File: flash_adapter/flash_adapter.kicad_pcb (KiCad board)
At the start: 2 copper layers, 47 x 53.3 mm, 4 parts, among them J1 Conn_02x12_Odd_Even, J2 Conn_02x12_Odd_Even, J4 Conn_01x04_Pin, U1 Kickstart_Socket_A4000

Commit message: finish routing
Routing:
- net /L18: track 0.00 -> 45.9 mm, vias 0 -> 1
- net /L8: track 0.00 -> 45.5 mm, vias 0 -> 1
- net /R15: track 0.00 -> 44.8 mm, vias 0 -> 2
- net /R16: track 0.00 -> 43.1 mm, vias 0 -> 2
- net /L7: track 0.00 -> 43.0 mm, vias 0 -> 1
- net /R24: track 0.00 -> 42.7 mm, vias 0 -> 2
- net /L20: track 0.00 -> 40.6 mm, vias 0 -> 1
- net /R21: track 0.00 -> 40.2 mm, vias 0 -> 2
- net /L6: track 0.00 -> 39.6 mm, vias 0 -> 2
- net /L17: track 0.00 -> 38.1 mm, vias 0 -> 1
- net /L5: track 0.00 -> 37.9 mm, vias 0 -> 2
- net /L22: track 0.00 -> 37.9 mm, vias 0 -> 2
- net /R17: track 0.00 -> 36.7 mm, vias 0 -> 2
- net /R23: track 15.1 -> 51.2 mm, vias 0 -> 2
- net /L12: track 0.00 -> 35.7 mm, vias 0 -> 1
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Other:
- board text added: "1"

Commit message: increase silkscreen line width; manufacturability
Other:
- board text added: "Flashrom programming adapter"
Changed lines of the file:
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@@
     )
     (pad_to_mask_clearance 0)
+    (aux_axis_origin 79.375 66.04)
     (pcbplotparams
-      (layerselection 0x00010fc_ffffffff)
+      (layerselection 0x00010ec_ffffffff)
       (plot_on_all_layers_selection 0x0000000_00000000)
       (disableapertmacros false)
-      (usegerberextensions false)
-      (usegerberattributes true)
-      (usegerberadvancedattributes true)
-      (creategerberjobfile true)
+      (usegerberextensions true)
+      (usegerberattributes false)
+      (usegerberadvancedattributes false)
+      (creategerberjobfile false)
       (dashed_line_dash_ratio 12.000000)
       (dashed_line_gap_ratio 3.000000)
@@
       (psa4output false)
       (plotreference true)
-      (plotvalue true)
+      (plotvalue false)
       (plotinvisibletext false)
       (sketchpadsonfab false)
-      (subtractmaskfromsilk false)
+      (subtractmaskfromsilk true)
       (outputformat 1)
       (mirror false)
-      (drillshape 1)
+      (drillshape 0)
       (scaleselection 1)
-      (outputdirectory "")
+      (outputdirectory "output/")
     )
   )
@@
     (property "ki_keywords" "ROM SOKCET")
     (attr through_hole)
-    (fp_text reference "U1" (at 7.62 2.54) (layer "F.SilkS")
+    (fp_text reference "U1" (at 7.62 2.54 unlocked) (layer "F.SilkS")
         (effects (font (size 1 1) (thickness 0.15)))
     )
@@
     (property "ki_keywords" "connector")
     (attr through_hole)
-    (fp_text reference "J2" (at -1.27 31.115) (layer "F.SilkS")
+    (fp_text reference "J2" (at -1.27 31.115 unlocked) (layer "F.SilkS")
         (effects (font (size 1 1) (thickness 0.15)))
     )
@@
     (property "ki_keywords" "connector")
     (attr through_hole)
-    (fp_text reference "J4" (at 2.79 3.81 -180) (layer "F.SilkS")
+    (fp_text reference "J4" (at 2.79 3.81 unlocked) (layer "F.SilkS")
         (effects (font (size 1 1) (thickness 0.15)))
     )
@@
     (property "ki_keywords" "connector")
     (attr through_hole)
-    (fp_text reference "J1" (at -1.27 31.115) (layer "F.SilkS")
+    (fp_text reference "J1" (at -1.27 31.115 unlocked) (layer "F.SilkS")
         (effects (font (size 1 1) (thickness 0.15)))
     )
@@
   )
   (gr_line (start 103.505 67.945) (end 103.505 66.675)
-    (stroke (width 0.1) (type default)) (layer "F.SilkS"))
+    (stroke (width 0.15) (type default)) (layer "F.SilkS"))
   (gr_line (start 102.235 66.675) (end 102.235 67.945)
-    (stroke (width 0.1) (type default)) (layer "F.SilkS"))
+    (stroke (width 0.15) (type default)) (layer "F.SilkS"))
   (gr_line (start 103.505 66.675) (end 104.775 66.675)
-    (stroke (width 0.1) (type default)) (layer "F.SilkS"))
+    (stroke (width 0.15) (type default)) (layer "F.SilkS"))
   (gr_line (start 104.775 66.675) (end 102.87 64.77)
-    (stroke (width 0.1) (type default)) (layer "F.SilkS"))
+    (stroke (width 0.15) (type default)) (layer "F.SilkS"))
   (gr_line (start 100.965 66.675) (end 102.235 66.675)
-    (stroke (width 0.1) (type default)) (layer "F.SilkS"))
+    (stroke (width 0.15) (type default)) (layer "F.SilkS"))
   (gr_line (start 102.87 64.77) (end 100.965 66.675)
-    (stroke (width 0.1) (type default)) (layer "F.SilkS"))
+    (stroke (width 0.15) (type default)) (layer "F.SilkS"))
   (gr_line (start 102.235 67.945) (end 103.505 67.945)
-    (stroke (width 0.1) (type default)) (layer "F.SilkS"))
+    (stroke (width 0.15) (type default)) (layer "F.SilkS"))
   (gr_line (start 110.5 116.84) (end 63.5 116.84)
     (stroke (width 0.05) (type default)) (layer "Edge.Cuts"))
@@
   (gr_line (start 63.5 63.5) (end 110.5 63.5)
     (stroke (width 0.05) (type default)) (layer "Edge.Cuts"))
+  (gr_text "Flashrom\nprogramming\nadapter" (at 64.77 114.935) (layer "F.SilkS")
+    (effects (font (size 1.2 1) (thickness 0.15)) (justify left bottom))
+  )
   (gr_text "1" (at 75.565 66.675) (layer "F.SilkS")
     (effects (font (size 1.5 1.5) (thickness 0.2)) (justify left bottom))

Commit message: add J4 silkscreen pin descriptions
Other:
- board text added: "~{WE} ~{RESET} RY/~{BY} A18"
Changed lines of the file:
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@@
     (property "ki_keywords" "connector")
     (attr through_hole)
-    (fp_text reference "J4" (at 2.79 3.81 unlocked) (layer "F.SilkS")
+    (fp_text reference "J4" (at -2.925 3.81 unlocked) (layer "F.SilkS")
         (effects (font (size 1 1) (thickness 0.15)))
     )
@@
   (gr_line (start 63.5 63.5) (end 110.5 63.5)
     (stroke (width 0.05) (type default)) (layer "Edge.Cuts"))
+  (gr_text "~{WE}\n~{RESET}\nRY/~{BY}\nA18" (at 81.915 100.965 270) (layer "F.SilkS")
+    (effects (font (size 1.6 1.5) (thickness 0.15)) (justify left bottom))
+  )
   (gr_text "Flashrom\nprogramming\nadapter" (at 64.77 114.935) (layer "F.SilkS")
     (effects (font (size 1.2 1) (thickness 0.15)) (justify left bottom))

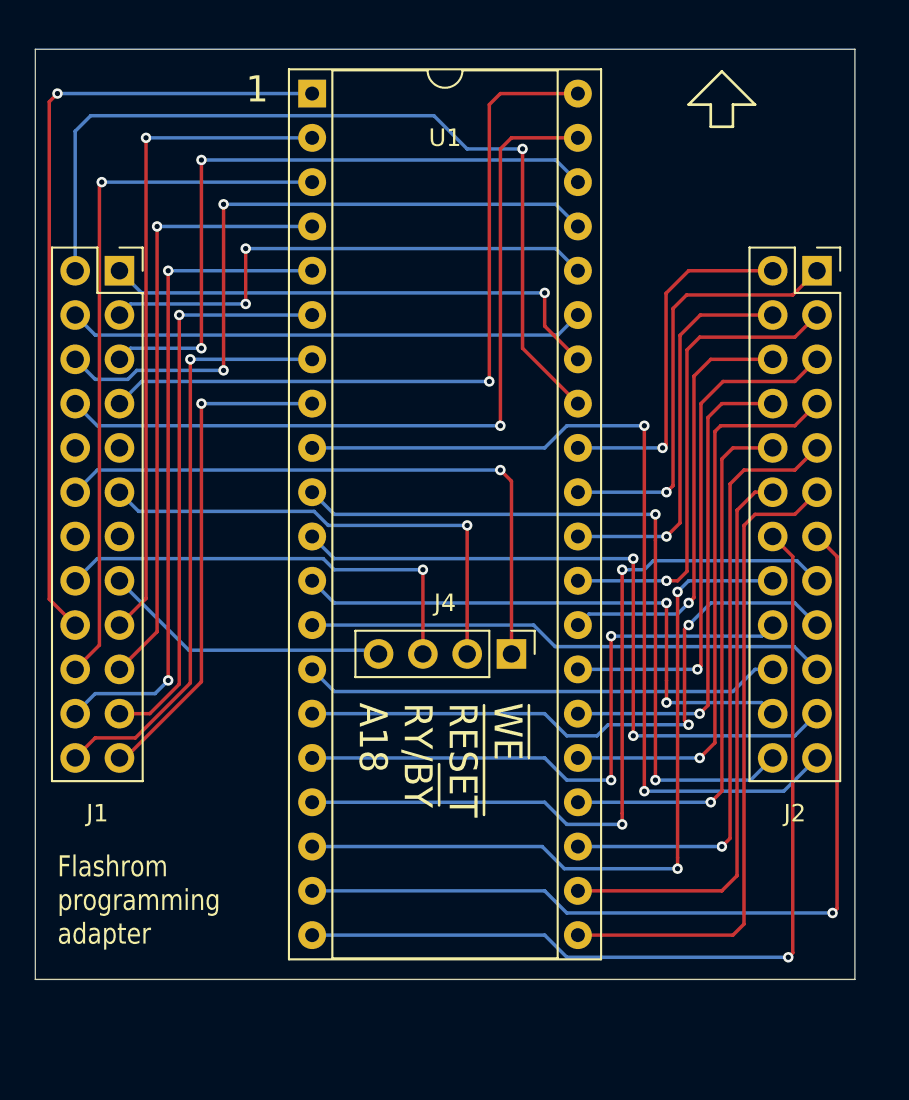
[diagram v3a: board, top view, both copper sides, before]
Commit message: increase dip 40 socket hole size in order to allow use of textool socket
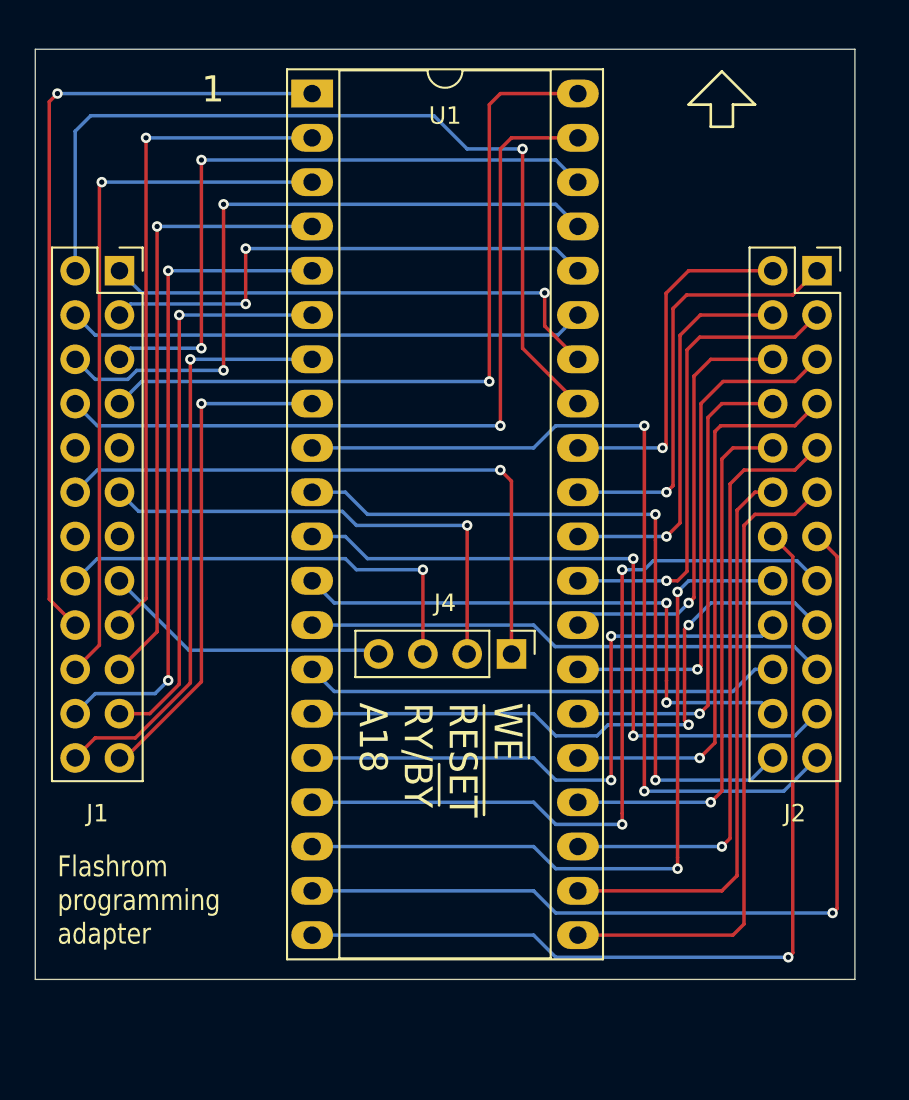
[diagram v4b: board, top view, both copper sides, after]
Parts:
- U1: footprint Package_DIP:DIP-40_W15.24mm_Socket -> Package_DIP:DIP-40_W15.24mm_Socket_LongPads

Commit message: relocate header for non-socket signals to next to socket to avoid through holes under textool
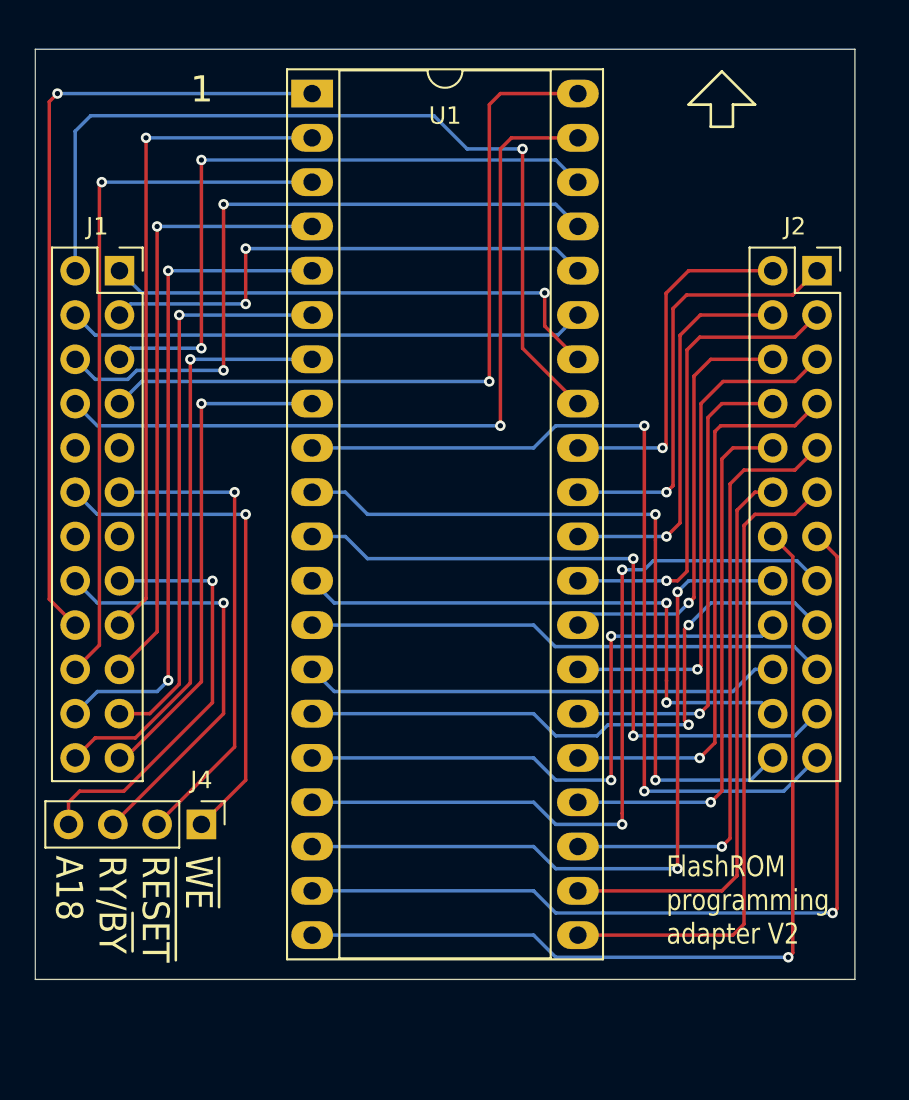
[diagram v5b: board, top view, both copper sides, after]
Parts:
- moved J4 20.3 mm to (73.0, 108.0)
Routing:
- net /A18: track 16.6 -> 24.2 mm, vias 0 -> 1
- net /L12: track 35.7 -> 29.1 mm
- net /L16: track 25.6 -> 24.4 mm
- net /L11: track 28.1 -> 27.5 mm
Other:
- board text added: "FlashROM programming adapter V2"
- board text removed: "Flashrom programming adapter"
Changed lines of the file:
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@@
     (property "ki_keywords" "connector")
     (attr through_hole)
-    (fp_text reference "J2" (at -1.27 31.115 unlocked) (layer "F.SilkS")
+    (fp_text reference "J2" (at -1.27 -2.54 unlocked) (layer "F.SilkS")
         (effects (font (size 1 1) (thickness 0.15)))
     )
@@
   )
   (footprint "Connector_PinHeader_2.54mm:PinHeader_1x04_P2.54mm_Vertical" (layer "F.Cu")
-    (at 90.805 98.175 -90)
+    (at 73.025 107.95 -90)
     (descr "Through hole straight pin header, 1x04, 2.54mm pitch, single row")
     (tags "Through hole pin header THT 1x04 2.54mm single row")
@@
     (property "ki_keywords" "connector")
     (attr through_hole)
-    (fp_text reference "J4" (at -2.925 3.81 unlocked) (layer "F.SilkS")
+    (fp_text reference "J4" (at -2.54 0 unlocked) (layer "F.SilkS")
         (effects (font (size 1 1) (thickness 0.15)))
     )
@@
     (property "ki_keywords" "connector")
     (attr through_hole)
-    (fp_text reference "J1" (at -1.27 31.115 unlocked) (layer "F.SilkS")
+    (fp_text reference "J1" (at -1.27 -2.54 unlocked) (layer "F.SilkS")
         (effects (font (size 1 1) (thickness 0.15)))
     )
@@
   (gr_line (start 63.5 63.5) (end 110.5 63.5)
     (stroke (width 0.05) (type default)) (layer "Edge.Cuts"))
-  (gr_text "~{WE}\n~{RESET}\nRY/~{BY}\nA18" (at 81.915 100.965 270) (layer "F.SilkS")
-    (effects (font (size 1.6 1.5) (thickness 0.15)) (justify left bottom))
-  )
-  (gr_text "Flashrom\nprogramming\nadapter" (at 64.77 114.935) (layer "F.SilkS")
+  (gr_text "~{WE}\n~{RESET}\nRY/~{BY}\nA18" (at 64.516 109.728 270) (layer "F.SilkS")
+    (effects (font (size 1.54 1.4) (thickness 0.15)) (justify left bottom))
+  )
+  (gr_text "FlashROM\nprogramming\nadapter V2" (at 99.695 114.935) (layer "F.SilkS")
     (effects (font (size 1.2 1) (thickness 0.15)) (justify left bottom))
   )
-  (gr_text "1" (at 73.025 66.675) (layer "F.SilkS")
+  (gr_text "1" (at 72.39 66.675) (layer "F.SilkS")
     (effects (font (size 1.5 1.5) (thickness 0.2)) (justify left bottom))
   )
@@
   (segment (start 65.786 83.82) (end 67.056 85.09) (width 0.2) (layer "B.Cu") (net 8))
   (segment (start 67.056 85.09) (end 90.17 85.09) (width 0.2) (layer "B.Cu") (net 8))
-  (segment (start 88.265 98.175) (end 88.265 90.805) (width 0.2) (layer "F.Cu") (net 11))
-  (via (at 88.265 90.805) (size 0.6) (drill 0.3) (layers "F.Cu" "B.Cu") (net 11))
-  (segment (start 81.915 90.805) (end 81.11 90) (width 0.2) (layer "B.Cu") (net 11))
-  (segment (start 69.426 90) (end 68.326 88.9) (width 0.2) (layer "B.Cu") (net 11))
-  (segment (start 81.11 90) (end 69.426 90) (width 0.2) (layer "B.Cu") (net 11))
-  (segment (start 88.265 90.805) (end 81.915 90.805) (width 0.2) (layer "B.Cu") (net 11))
-  (segment (start 90.805 98.175) (end 90.805 88.265) (width 0.2) (layer "F.Cu") (net 12))
-  (segment (start 90.805 88.265) (end 90.17 87.63) (width 0.2) (layer "F.Cu") (net 12))
-  (via (at 90.17 87.63) (size 0.6) (drill 0.3) (layers "F.Cu" "B.Cu") (net 12))
-  (segment (start 67.056 87.63) (end 65.786 88.9) (width 0.2) (layer "B.Cu") (net 12))
-  (segment (start 90.17 87.63) (end 67.056 87.63) (width 0.2) (layer "B.Cu") (net 12))
-  (segment (start 72.306 97.96) (end 68.326 93.98) (width 0.2) (layer "B.Cu") (net 15))
-  (segment (start 82.97 97.96) (end 72.306 97.96) (width 0.2) (layer "B.Cu") (net 15))
-  (segment (start 83.185 98.175) (end 82.97 97.96) (width 0.2) (layer "B.Cu") (net 15))
-  (segment (start 85.725 93.345) (end 85.725 98.175) (width 0.2) (layer "F.Cu") (net 16))
-  (via (at 85.725 93.345) (size 0.6) (drill 0.3) (layers "F.Cu" "B.Cu") (net 16))
-  (segment (start 65.786 93.98) (end 67.056 92.71) (width 0.2) (layer "B.Cu") (net 16))
-  (segment (start 81.28 92.71) (end 81.915 93.345) (width 0.2) (layer "B.Cu") (net 16))
-  (segment (start 81.915 93.345) (end 85.725 93.345) (width 0.2) (layer "B.Cu") (net 16))
-  (segment (start 67.056 92.71) (end 81.28 92.71) (width 0.2) (layer "B.Cu") (net 16))
+  (segment (start 74.93 103.505) (end 70.485 107.95) (width 0.2) (layer "F.Cu") (net 11))
+  (segment (start 74.93 88.9) (end 74.93 103.505) (width 0.2) (layer "F.Cu") (net 11))
+  (via (at 74.93 88.9) (size 0.6) (drill 0.3) (layers "F.Cu" "B.Cu") (net 11))
+  (segment (start 74.93 88.9) (end 68.326 88.9) (width 0.2) (layer "B.Cu") (net 11))
+  (segment (start 75.565 105.41) (end 75.565 90.17) (width 0.2) (layer "F.Cu") (net 12))
+  (segment (start 73.025 107.95) (end 75.565 105.41) (width 0.2) (layer "F.Cu") (net 12))
+  (via (at 75.565 90.17) (size 0.6) (drill 0.3) (layers "F.Cu" "B.Cu") (net 12))
+  (segment (start 75.565 90.17) (end 67.056 90.17) (width 0.2) (layer "B.Cu") (net 12))
+  (segment (start 67.056 90.17) (end 65.786 88.9) (width 0.2) (layer "B.Cu") (net 12))
+  (segment (start 66.04 106.045) (end 65.405 106.68) (width 0.2) (layer "F.Cu") (net 15))
+  (segment (start 73.66 100.965) (end 68.58 106.045) (width 0.2) (layer "F.Cu") (net 15))
+  (segment (start 73.66 93.98) (end 73.66 100.965) (width 0.2) (layer "F.Cu") (net 15))
+  (segment (start 65.405 106.68) (end 65.405 107.95) (width 0.2) (layer "F.Cu") (net 15))
+  (segment (start 68.58 106.045) (end 66.04 106.045) (width 0.2) (layer "F.Cu") (net 15))
+  (via (at 73.66 93.98) (size 0.6) (drill 0.3) (layers "F.Cu" "B.Cu") (net 15))
+  (segment (start 73.66 93.98) (end 68.326 93.98) (width 0.2) (layer "B.Cu") (net 15))
+  (segment (start 74.295 101.6) (end 67.945 107.95) (width 0.2) (layer "F.Cu") (net 16))
+  (segment (start 74.295 101.6) (end 74.295 95.25) (width 0.2) (layer "F.Cu") (net 16))
+  (via (at 74.295 95.25) (size 0.6) (drill 0.3) (layers "F.Cu" "B.Cu") (net 16))
+  (segment (start 74.295 95.25) (end 67.056 95.25) (width 0.2) (layer "B.Cu") (net 16))
+  (segment (start 67.056 95.25) (end 65.786 93.98) (width 0.2) (layer "B.Cu") (net 16))
   (segment (start 69.85 94.996) (end 68.326 96.52) (width 0.2) (layer "F.Cu") (net 17))
   (segment (start 69.85 68.58) (end 69.85 94.996) (width 0.2) (layer "F.Cu") (net 17))
@@
   (via (at 70.485 73.66) (size 0.6) (drill 0.3) (layers "F.Cu" "B.Cu") (net 19))
   (segment (start 79.375 73.66) (end 70.485 73.66) (width 0.2) (layer "B.Cu") (net 19))
+  (segment (start 67.176 97.67) (end 65.786 99.06) (width 0.2) (layer "F.Cu") (net 20))
+  (segment (start 67.176 71.254) (end 67.176 97.67) (width 0.2) (layer "F.Cu") (net 20))
   (segment (start 67.31 71.12) (end 67.176 71.254) (width 0.2) (layer "F.Cu") (net 20))
-  (segment (start 67.176 71.254) (end 67.176 97.67) (width 0.2) (layer "F.Cu") (net 20))
-  (segment (start 67.176 97.67) (end 65.786 99.06) (width 0.2) (layer "F.Cu") (net 20))
   (via (at 67.31 71.12) (size 0.6) (drill 0.3) (layers "F.Cu" "B.Cu") (net 20))
   (segment (start 79.375 71.12) (end 67.31 71.12) (width 0.2) (layer "B.Cu") (net 20))
@@
   (via (at 71.12 99.695) (size 0.6) (drill 0.3) (layers "F.Cu" "B.Cu") (net 22))
   (segment (start 79.375 76.2) (end 71.12 76.2) (width 0.2) (layer "B.Cu") (net 22))
-  (segment (start 66.936 100.45) (end 65.786 101.6) (width 0.2) (layer "B.Cu") (net 22))
-  (segment (start 70.365 100.45) (end 66.936 100.45) (width 0.2) (layer "B.Cu") (net 22))
-  (segment (start 71.12 99.695) (end 70.365 100.45) (width 0.2) (layer "B.Cu") (net 22))
+  (segment (start 70.485 100.33) (end 67.056 100.33) (width 0.2) (layer "B.Cu") (net 22))
+  (segment (start 71.12 99.695) (end 70.485 100.33) (width 0.2) (layer "B.Cu") (net 22))
+  (segment (start 67.056 100.33) (end 65.786 101.6) (width 0.2) (layer "B.Cu") (net 22))
   (segment (start 68.6549 104.14) (end 68.326 104.14) (width 0.2) (layer "F.Cu") (net 23))
   (segment (start 73.025 83.82) (end 73.025 99.7699) (width 0.2) (layer "F.Cu") (net 23))
